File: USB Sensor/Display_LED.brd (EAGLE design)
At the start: 160 x 100 mm, 7 parts, among them U1 ATMEGA644M, U3 TLV61220DBV

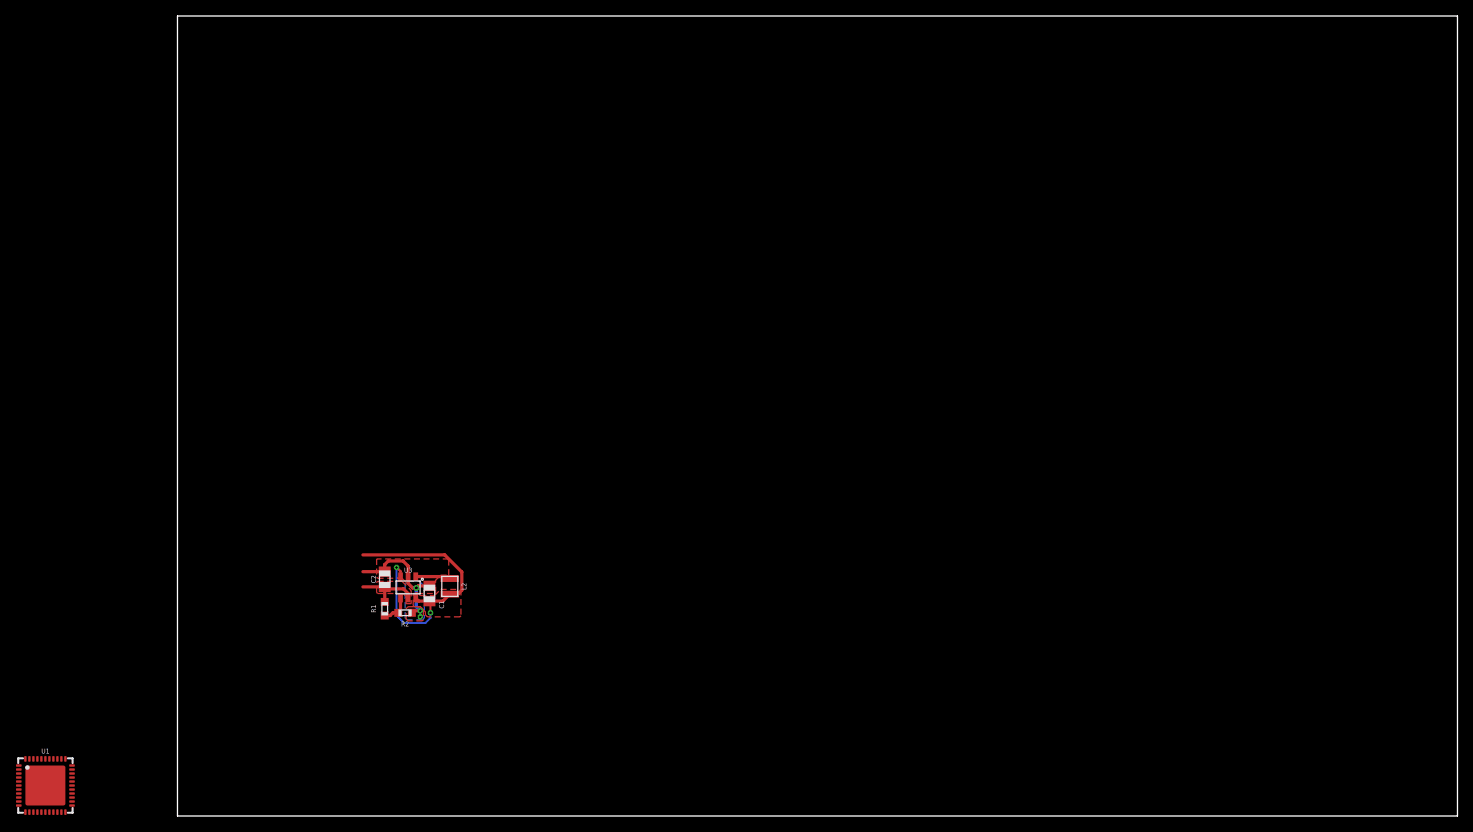
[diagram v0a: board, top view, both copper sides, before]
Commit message: Continued layout of display module
Preliminary placement done, major layout remaining
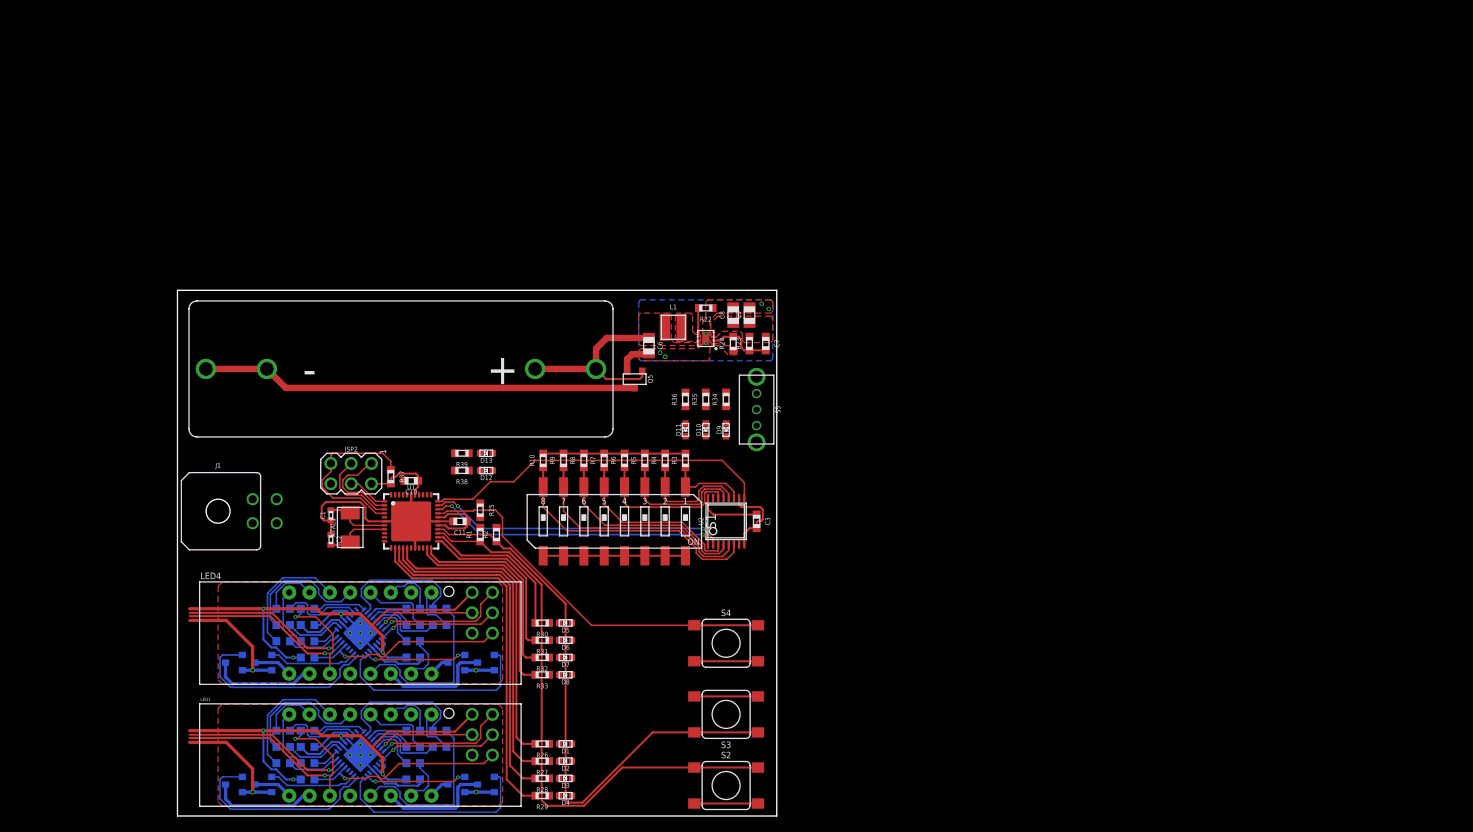
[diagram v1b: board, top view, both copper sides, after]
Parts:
- removed L2: 6.8uH, bschulz:1008
- removed U3: TLV61220DBV, bschulz:DBV_R-PDSO-G6
- added BT1: AACLIP, bschulz:BAT_AA
- added C10, C13, C5: 1uF, bschulz_passives:C0603
- added C11, C12, C3, C4: 0.1uF, bschulz_passives:C0603
- added C6: 10uF, bschulz_passives:C0805
- added C7: 10pF, bschulz_passives:C0603
- added C8, C9: 4.7uF, bschulz_passives:C0805
- added D1, D10, D11, D12, D13, D2, D3, D4, D5, D6, D7, D8, D9: LED0603, bschulz:LED_0603
- added ISP1, ISP2, ISP4: AVRISP-6, bschulz:AVRISP
- added J1: (no value), bschulz:2X2_MICROFIT_RT
- added L1: (no value), bschulz:WE-MAPI(3X3)
- added LED1, LED4: YSD-439AR6B-35, SparkFun-LED:7-SEGMENT-4DIGIT-YOUNGSUN
- added Q1, Q13, Q14, Q15, Q16, Q2, Q3, Q4: MOSFET-NCH-2N7002P, bschulz:SOT23-3
- added Q5: MOSFET-NCH-ZXMN3B14FTA, bschulz:SOT23-3
- added R10, R22, R24, R3, R4, R5, R6, R7, R8, R9: 100k, bschulz_passives:R0603
- added R11, R37, R45: 10k, bschulz_passives:R0603
- added R12, R13, R14, R15, R16, R17, R18, R19, R20, R21, R25, R26, R27, R28, R29, R30, R31, R32, R33, R35, R36, R38, R39, R46, R47, R48, R49, R50, R51, R52, R53, R54, R55: (no value), bschulz_passives:R0603
- added R23: 316k, bschulz_passives:R0603
- added R34: 330R, bschulz_passives:R0603
- added S1: DIP_8219_GULL, bschulz:219-8_GULLWING_DIP-CTS
- added S2, S3, S4: BUTTON6X6, bschulz:SWITCH_6MM
- added S5: SPDTOS1020, bschulz:OS102011MS2QN1
- added U2: (no value), bschulz:TSSOP16
- added U4, U7: ATMEGA48PMLF, bschulz:MLF32-5X5
- added U5: TPS61021A, bschulz:DSG0008A
- added XTAL1: CRYSTAL8MHZ5X3.2, bschulz:CRYSTAL_5X3.2_2-SMD
- C1, C2: value 10uF -> (none); device bschulz_passives:C0805 -> bschulz_passives:C0402
- R1: value 1M -> (none)
- R2: value 180k -> (none)
- moved U1 56.4 mm to (29.2, 36.8)
- moved C1 15.7 mm to (19.2, 37.6)
- moved R1 15.1 mm to (37.8, 35.2)
- moved R2 15.0 mm to (39.9, 35.2), turned to 90 degrees
- moved C2 8.36 mm to (19.2, 34.5), turned to 270 degrees
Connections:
- removed net AVCC: U1.27
- removed net EXP: U1.TH
- removed net FB1: R1.1, R2.2, U3.4
- removed net RX0: U1.9
- removed net SW1: L2.2, U3.1
- removed net TX0: U1.10
- removed net VCC: U1.17, U1.38, U1.5
- removed net VIN: C1.1, L2.1, U3.3, U3.6
- new net !RESET: ISP2.5, R37.1, U1.4
- new net !RESET_A: ISP1.5, R11.1, U4.29
- new net !RESET_B: ISP4.5, R45.1, U7.29
- new net B0: R3.1, S1.16, U2.11
- new net B1: R4.1, S1.15, U2.12
- new net B2: R5.1, S1.14, U2.13
- new net B3: R6.1, S1.13, U2.14
- new net B4: R7.1, S1.12, U2.3
- new net B5: R8.1, S1.11, U2.4
- new net B6: R9.1, S1.10, U2.5
- new net B7: R10.1, S1.9, U2.6
- new net BAT: BT1.POS@1, BT1.POS@2, C6.1, L1.P$1, Q5.1, R34.2, S5.1, U5.8
- new net BOOST_EN: R22.2, S5.2, U5.5
- new net DIP_CLK: U1.32, U2.2
- new net DIP_LD: U1.31, U2.1
- new net DIP_OUT: U1.33, U2.9
- new net DISP_SEL_A: R1.1, S2.1, S2.2, U1.25
- new net DISP_SEL_B: R2.1, S3.1, S3.2, U1.26
- new net DISP_STAT_D1_A: R28.2, U1.14
- new net DISP_STAT_D1_B: R32.2, U1.22
- new net DISP_STAT_D2_A: R29.2, U1.13
- new net DISP_STAT_D2_B: R33.2, U1.21
- new net DISP_STAT_I_A: R27.2, U1.15
- new net DISP_STAT_I_B: R31.2, U1.23
- new net DISP_STAT_V_A: R26.2, U1.16
- new net DISP_STAT_V_B: R30.2, U1.24
- new net DIS_A1: LED1.14, R12.1
- new net DIS_A2: LED4.14, R46.1
- new net DIS_B1: LED1.16, R13.1
- new net DIS_B2: LED4.16, R47.1
- new net DIS_C1: LED1.13, R14.1
- new net DIS_C2: LED4.13, R48.1
- new net DIS_COL1: LED1.12, R20.1
- new net DIS_COL2: LED4.12, R54.1
- new net DIS_D1: LED1.3, R15.1
- new net DIS_D2: LED4.3, R49.1
- new net DIS_DIG1_1: LED1.1, Q1.3
- new net DIS_DIG1_2: LED4.1, Q13.3
- new net DIS_DIG2_1: LED1.2, Q2.3
- new net DIS_DIG2_2: LED4.2, Q14.3
- new net DIS_DIG3_1: LED1.6, Q3.3
- new net DIS_DIG3_2: LED4.6, Q15.3
- new net DIS_DIG4_1: LED1.8, Q4.3
- new net DIS_DIG4_2: LED4.8, Q16.3
- new net DIS_DP1: LED1.7, R19.1
- new net DIS_DP2: LED4.7, R53.1
- new net DIS_E1: LED1.5, R16.1
- new net DIS_E2: LED4.5, R50.1
- new net DIS_F1: LED1.11, R17.1
- new net DIS_F2: LED4.11, R51.1
- new net DIS_G1: LED1.15, R18.1
- new net DIS_G2: LED4.15, R52.1
- new net DIS_POS1: LED1.9, R21.1
- new net DIS_POS2: LED4.9, R55.1
- new net FB: C7.2, R23.1, R24.2, U5.2
- new net HOLD: R25.1, S4.1, S4.2, U1.30
- new net MCU_A1: R12.2, U4.32
- new net MCU_A2: R46.2, U7.32
- new net MCU_B1: R13.2, U4.1
- new net MCU_B2: R47.2, U7.1
- new net MCU_C1: R14.2, U4.2
- new net MCU_C2: R48.2, U7.2
- new net MCU_COL1: R20.2, U4.12
- new net MCU_COL2: R54.2, U7.12
- new net MCU_D1: R15.2, U4.9
- new net MCU_D2: R49.2, U7.9
- new net MCU_DIG1_1: Q1.1, U4.26
- new net MCU_DIG1_2: Q13.1, U7.26
- new net MCU_DIG2_1: Q2.1, U4.25
- new net MCU_DIG2_2: Q14.1, U7.25
- new net MCU_DIG3_1: Q3.1, U4.24
- new net MCU_DIG3_2: Q15.1, U7.24
- new net MCU_DIG4_1: Q4.1, U4.23
- new net MCU_DIG4_2: Q16.1, U7.23
- new net MCU_DP1: R19.2, U4.14
- new net MCU_DP2: R53.2, U7.14
- new net MCU_E1: R16.2, U4.10
- new net MCU_E2: R50.2, U7.10
- new net MCU_F1: R17.2, U4.11
- new net MCU_F2: R51.2, U7.11
- new net MCU_G1: R18.2, U4.7
- new net MCU_G2: R52.2, U7.7
- new net MCU_POS1: R21.2, U4.13
- new net MCU_POS2: R55.2, U7.13
- new net MISO_A: ISP1.1, U4.16
- new net MISO_B: ISP4.1, U7.16
- new net MOSI_A: ISP1.4, U4.15
- new net MOSI_B: ISP4.4, U7.15
- new net N$1: D1.ANODE, R26.1
- new net N$10: BT1.NEG@1, BT1.NEG@2, D9.ANODE, Q5.3
- new net N$11: D9.CATHODE, R34.1
- new net N$12: D12.ANODE, R38.1
- new net N$13: C2.2, U1.8, XTAL1.OSC1
- new net N$14: D11.ANODE, R36.1
- new net N$15: C1.2, U1.7, XTAL1.OSC2
- new net N$16: D13.ANODE, R39.1
- new net N$2: D2.ANODE, R27.1
- new net N$21: U1.34
- new net N$22: U1.35
- new net N$23: U1.36
- new net N$24: U1.37
- new net N$3: D3.ANODE, R28.1
- new net N$4: D4.ANODE, R29.1
- new net N$5: D5.ANODE, R30.1
- new net N$6: D6.ANODE, R31.1
- new net N$7: D7.ANODE, R32.1
- new net N$8: D8.ANODE, R33.1
- new net N$9: D10.ANODE, R35.1
- new net PG: R36.2
- new net RX2: U1.12, U7.30
- new net SCK_A: ISP1.3, U4.17
- new net SCK_B: ISP4.3, U7.17
- new net STAT1: R39.2
- new net STAT2: R38.2
- new net SW: L1.P$2, U5.6, U5.7
- new net TX2: U1.11, U7.31
- net 3V3: now also C10.1, C11.1, C12.1, C13.1, C3.1, C4.1, C5.1, C7.1, C8.1, C9.1, ISP1.2, ISP2.2, ISP4.2, R10.2, R11.2, R2.2, R23.2, R25.2, R3.2, R35.2, R37.2, R4.2, R45.2, R5.2, R6.2, R7.2, R8.2, R9.2, U1.17, U1.27, U1.29, U1.38, U1.5, U2.16, U4.18, U4.20, U4.4, U4.6, U5.3, U5.4, U7.18, U7.20, U7.4, U7.6; no longer C2.1, U3.5
- net GND: now also C1.1, C10.2, C11.2, C12.2, C13.2, C2.1, C3.2, C4.2, C5.2, C6.2, C8.2, C9.2, D1.CATHODE, D10.CATHODE, D11.CATHODE, D12.CATHODE, D13.CATHODE, D2.CATHODE, D3.CATHODE, D4.CATHODE, D5.CATHODE, D6.CATHODE, D7.CATHODE, D8.CATHODE, ISP1.6, ISP2.6, ISP4.6, LED1.10, LED1.4, LED4.10, LED4.4, Q1.2, Q13.2, Q14.2, Q15.2, Q16.2, Q2.2, Q3.2, Q4.2, Q5.2, R22.1, R24.1, S1.1, S1.2, S1.3, S1.4, S1.5, S1.6, S1.7, S1.8, S2.3, S2.4, S3.3, S3.4, S4.3, S4.4, S5.3, U1.TH, U2.10, U2.8, U4.21, U4.3, U4.5, U4.TH, U5.1, U5.EP@1, U5.EP@2, U5.EP@3, U7.21, U7.3, U7.5, U7.TH; no longer C1.2, C2.2, R2.1, U3.2
- net MISO: now also ISP2.1
- net MOSI: now also ISP2.4
- net RX1: now also U1.10, U4.30; no longer U1.11
- net SCK: now also ISP2.3
- net TX1: now also U1.9, U4.31; no longer U1.12
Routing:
- net 3V3: track 8.46 -> 174.3 mm, vias 0 -> 8
- net GND: track 17.1 -> 168.6 mm, vias 3 -> 18
- net DISP_SEL_B: track 0.00 -> 72.2 mm
- net DISP_SEL_A: track 0.00 -> 71.9 mm
- net N$10: track 0.00 -> 54.6 mm
- net HOLD: track 0.00 -> 47.5 mm
- net DISP_STAT_D2_A: track 0.00 -> 45.5 mm
- net DIP_OUT: track 0.00 -> 43.5 mm
- net DISP_STAT_D1_A: track 0.00 -> 43.1 mm
- net DISP_STAT_I_A: track 0.00 -> 40.7 mm
- net DISP_STAT_V_A: track 0.00 -> 38.4 mm
- net DIP_CLK: track 0.00 -> 37.2 mm, vias 0 -> 2
- net VIN: track 36.4 -> 0.00 mm, vias 2 -> 0
- net DIP_LD: track 0.00 -> 36.3 mm, vias 0 -> 2
- net B7: track 0.00 -> 33.2 mm
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- added copper zone on layer 1, net BAT
- added copper zone on layer 1, net SW
- removed copper zone on layer 1, net VIN
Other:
- board size 160 x 100 mm -> 74.9 x 65.7 mm

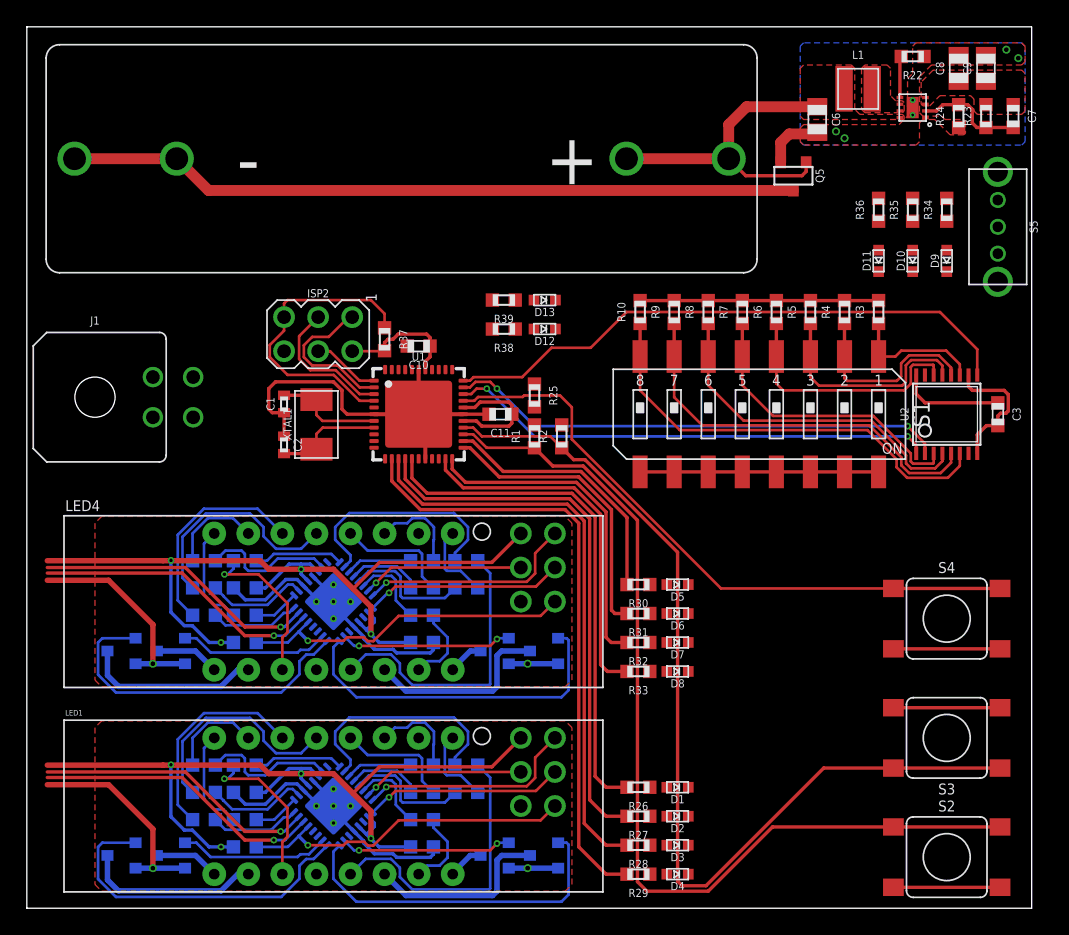
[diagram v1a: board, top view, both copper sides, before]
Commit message: Display layout complete, review required
Layout of display module is complete, should be reviewed before sending to fab
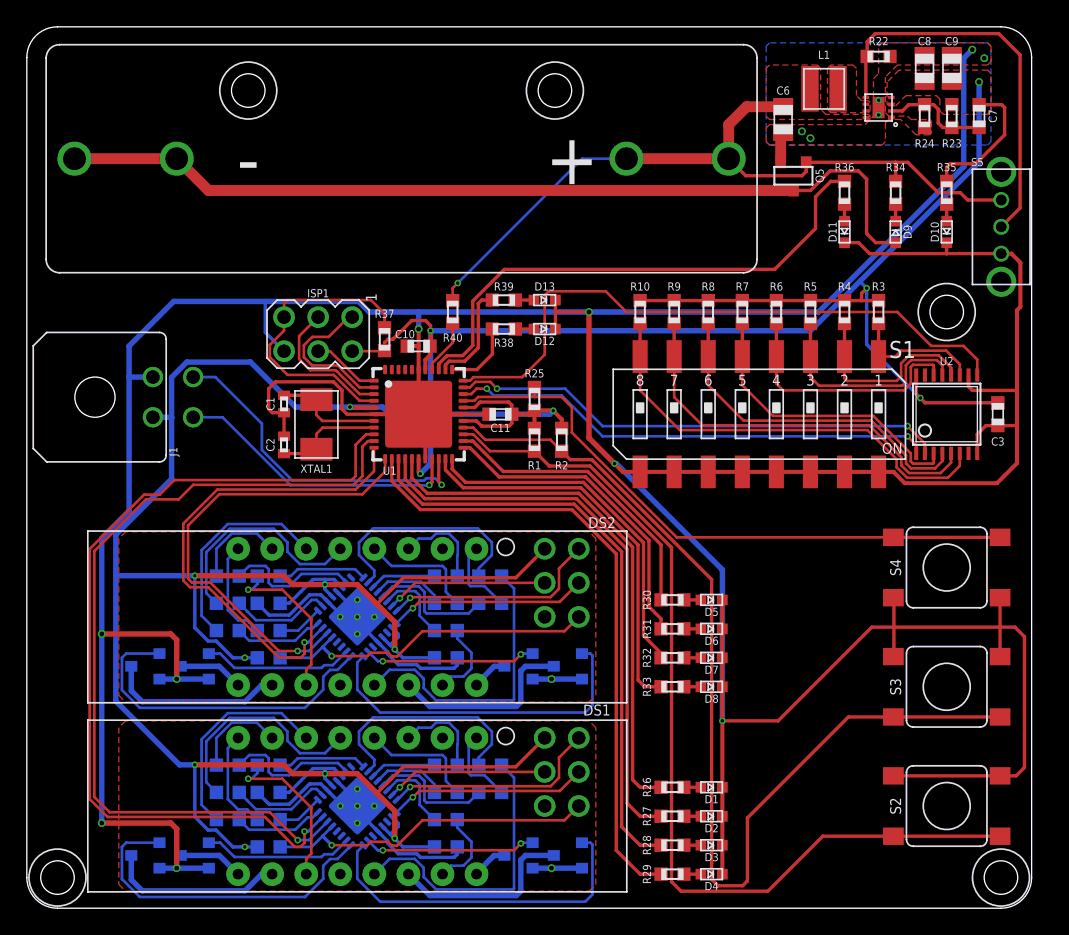
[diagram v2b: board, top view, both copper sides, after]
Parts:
- removed ISP4: AVRISP-6, bschulz:AVRISP
- removed LED1, LED4: YSD-439AR6B-35, SparkFun-LED:7-SEGMENT-4DIGIT-YOUNGSUN
- added DS1, DS2: YSD-439AK2B-35, bschulz:7-SEGMENT-4DIGIT-YOUNGSUN
- added H1, H2, H3, H4, H5: (no value), bschulz:2_56
- added ISP3: AVRISP-6, bschulz:AVRISP
- added R40: (no value), bschulz_passives:R0603
- BT1: device bschulz:BAT_AA -> bschulz:BAT_AA_BK-92
- moved ISP2 37.4 mm to (39.9, 10.2), flipped to the bottom, turned to 0 degrees
- moved ISP1 36.5 mm to (21.7, 42.8), flipped to the top, turned to 270 degrees
- moved D9 4.38 mm to (64.8, 50.4), turned to 270 degrees
- moved R34 4.02 mm to (64.8, 53.3)
- moved S3 3.81 mm to (68.6, 16.5)
- moved S2 3.81 mm to (68.6, 7.62), turned to 180 degrees
- moved S4 3.81 mm to (68.6, 25.4)
- moved D11 3.33 mm to (61.0, 50.4)
- moved D10 3.33 mm to (68.6, 50.4)
- moved R36 2.84 mm to (61.0, 53.3)
- moved R35 2.84 mm to (68.6, 53.3)
- moved D5 2.79 mm to (51.1, 23.0)
- moved D6 2.79 mm to (51.1, 20.8)
- moved D7 2.79 mm to (51.1, 18.7)
- moved R30 2.79 mm to (48.1, 23.0)
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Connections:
- removed net N$21: U1.34
- removed net N$22: U1.35
- removed net N$23: U1.36
- removed net N$24: U1.37
- new net BAT_SENSE: R40.1, U1.37
- net !RESET: now also ISP1.5; no longer ISP2.5
- net !RESET_A: now also ISP2.5; no longer ISP1.5
- net !RESET_B: now also ISP3.5; no longer ISP4.5
- net 3V3: now also ISP3.2, J1.1; no longer ISP4.2
- net BAT: now also R40.2
- net DIS_A1: now also DS1.14; no longer LED1.14
- net DIS_A2: now also DS2.14; no longer LED4.14
- net DIS_B1: now also DS1.16; no longer LED1.16
- net DIS_B2: now also DS2.16; no longer LED4.16
- net DIS_C1: now also DS1.13; no longer LED1.13
- net DIS_C2: now also DS2.13; no longer LED4.13
- net DIS_COL1: now also DS1.12; no longer LED1.12
- net DIS_COL2: now also DS2.12; no longer LED4.12
- net DIS_D1: now also DS1.3; no longer LED1.3
- net DIS_D2: now also DS2.3; no longer LED4.3
- net DIS_DIG1_1: now also DS1.1; no longer LED1.1
- net DIS_DIG1_2: now also DS2.1; no longer LED4.1
- net DIS_DIG2_1: now also DS1.2; no longer LED1.2
- net DIS_DIG2_2: now also DS2.2; no longer LED4.2
- net DIS_DIG3_1: now also DS1.6; no longer LED1.6
- net DIS_DIG3_2: now also DS2.6; no longer LED4.6
- net DIS_DIG4_1: now also DS1.8; no longer LED1.8
- net DIS_DIG4_2: now also DS2.8; no longer LED4.8
- net DIS_DP1: now also DS1.7; no longer LED1.7
- net DIS_DP2: now also DS2.7; no longer LED4.7
- net DIS_E1: now also DS1.5; no longer LED1.5
- net DIS_E2: now also DS2.5; no longer LED4.5
- net DIS_F1: now also DS1.11; no longer LED1.11
- net DIS_F2: now also DS2.11; no longer LED4.11
- net DIS_G1: now also DS1.15; no longer LED1.15
- net DIS_G2: now also DS2.15; no longer LED4.15
- net DIS_POS1: now also DS1.9; no longer LED1.9
- net DIS_POS2: now also DS2.9; no longer LED4.9
- net GND: now also DS1.10, DS1.4, DS2.10, DS2.4, ISP3.6, J1.2; no longer ISP4.6, LED1.10, LED1.4, LED4.10, LED4.4
- net MISO: now also ISP1.1; no longer ISP2.1
- net MISO_A: now also ISP2.1; no longer ISP1.1
- net MISO_B: now also ISP3.1; no longer ISP4.1
- net MOSI: now also ISP1.4; no longer ISP2.4
- net MOSI_A: now also ISP2.4; no longer ISP1.4
- net MOSI_B: now also ISP3.4; no longer ISP4.4
- net PG: now also U1.36
- net SCK: now also ISP1.3; no longer ISP2.3
- net SCK_A: now also ISP2.3; no longer ISP1.3
- net SCK_B: now also ISP3.3; no longer ISP4.3
- net SCL: now also J1.3
- net SDA: now also J1.4
- net STAT1: now also U1.35
- net STAT2: now also U1.34
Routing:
- net GND: track 168.6 -> 416.9 mm, vias 18 -> 24
- net 3V3: track 174.3 -> 322.1 mm, vias 8 -> 15
- net TX1: track 21.0 -> 65.0 mm
- net RX1: track 21.6 -> 63.2 mm
- net PG: track 0.00 -> 39.6 mm
- net BAT: track 24.4 -> 57.3 mm, vias 0 -> 1
- net BOOST_EN: track 3.10 -> 29.9 mm
- net SDA: track 0.00 -> 25.2 mm, vias 0 -> 1
- net SCL: track 0.00 -> 21.8 mm, vias 0 -> 1
- net TX2: track 21.0 -> 36.0 mm
- net RX2: track 21.6 -> 34.5 mm
- net N$10: track 54.6 -> 67.4 mm
- net STAT1: track 0.00 -> 7.79 mm
- net STAT2: track 0.00 -> 5.35 mm
- net BAT_SENSE: track 0.00 -> 4.08 mm
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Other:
- outline, holes or cut-outs redrawn
- board text added: "0"
- board text added: "1"
- board text added: "2"
- board text added: "3"
- board text added: "4"
- board text added: "5"
- board text added: "6"
- board text added: "7"
- board text added: "CSR Select"
- board text added: "Current"
- board text added: "DISP A"
- board text added: "DISP B"
- board text added: "DISPA"
- board text added: "DISPB"
- board text added: "HOLD"
- board text added: "OFF"
- board text added: "ON"
- board text added: "PG"
- board text added: "PWR"
- board text added: "Project Corvus Display - v0.0 Bobby Schulz"
- board text added: "RP"
- board text added: "SEL0"
- board text added: "SEL1"
- board text added: "To Sensor"
- board text added: "Voltage"
